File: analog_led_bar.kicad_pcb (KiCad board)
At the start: 2 copper layers, 71.4 x 22 mm, 13 parts, among them P1 SIG, U1 OPAMP_DR, U2 LM3914, U3 LM3914

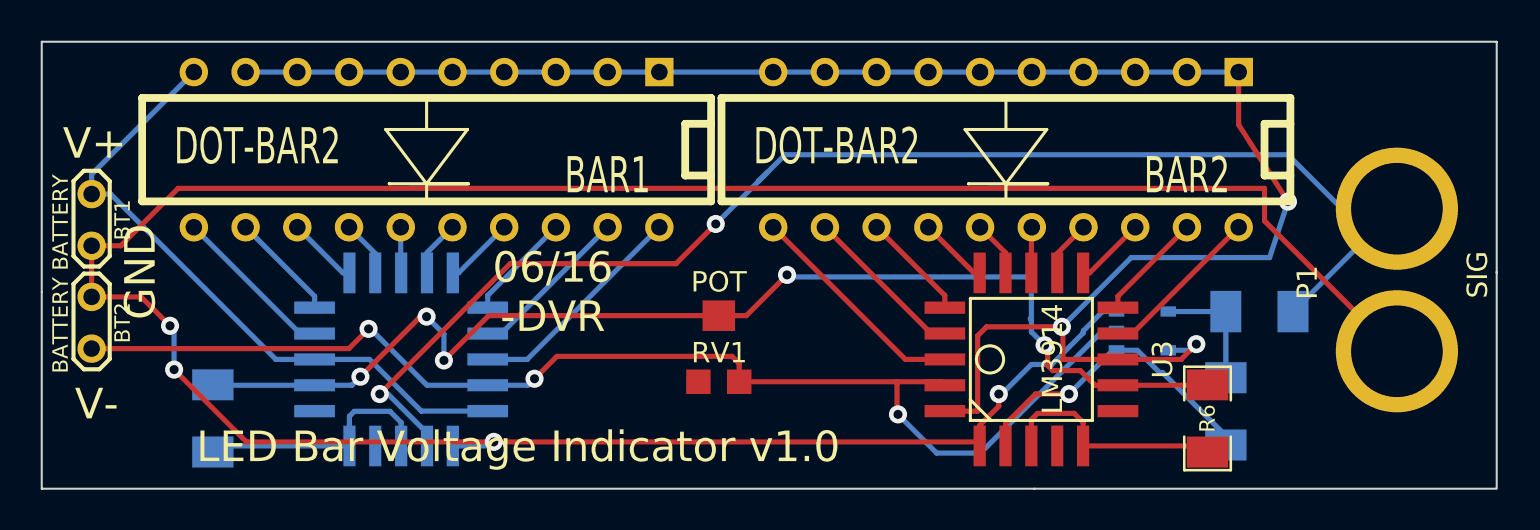
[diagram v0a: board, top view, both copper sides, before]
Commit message: Fixed unconnected nodes. Now v1.1. Confirmed works if variable resistor is set properly.
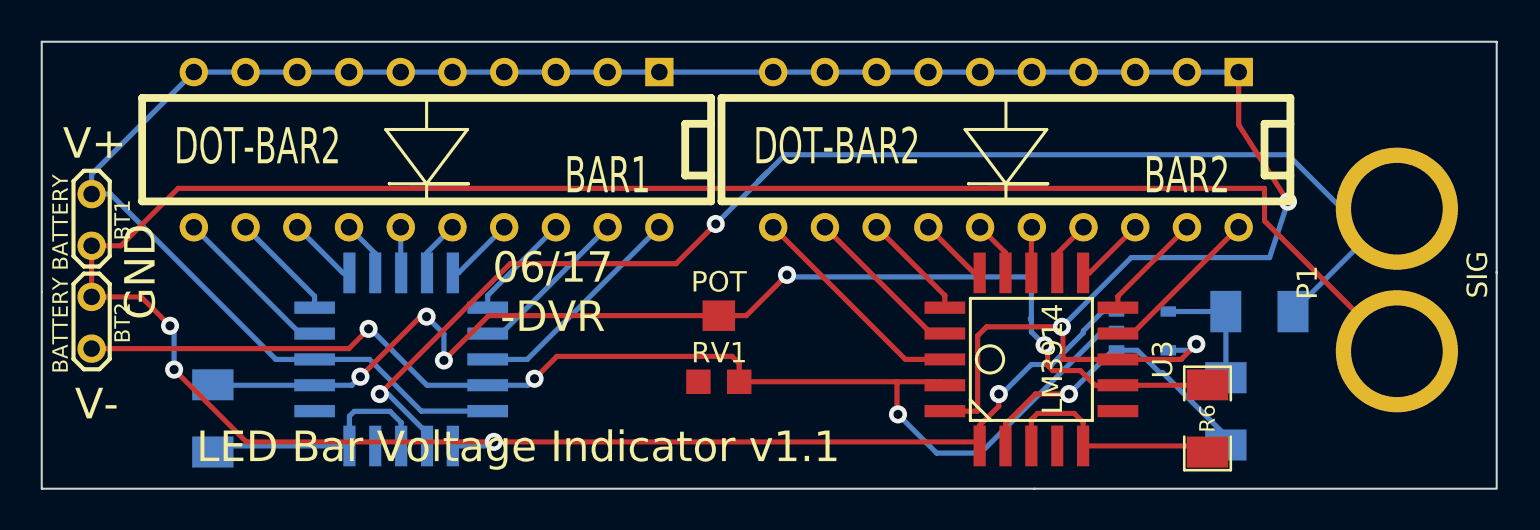
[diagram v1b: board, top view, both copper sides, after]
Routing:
- net /Vcc: track 121.9 -> 124.4 mm
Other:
- board text added: "06/17 -DVR"
- board text added: "LED Bar Voltage Indicator v1.1"
- board text removed: "06/16 -DVR"
- board text removed: "LED Bar Voltage Indicator v1.0"
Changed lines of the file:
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@@
   (general
     (links 68)
-    (no_connects 1)
+    (no_connects 0)
     (area 22.299999 12.699999 93.850001 34.750001)
     (thickness 1.6)
     (drawings 13)
-    (tracks 221)
+    (tracks 222)
     (zones 0)
     (modules 13)
@@
     (pad_to_mask_clearance 0)
     (aux_axis_origin 0 0)
-    (visible_elements FFFFFFBF)
+    (visible_elements 7FFFFFFF)
     (pcbplotparams
       (layerselection 285179905)
@@
     )
   )
-  (gr_text "06/16\n-DVR" (at 47.45 25.05) (layer F.SilkS)
+  (gr_text "06/17\n-DVR" (at 47.45 25.05) (layer F.SilkS)
     (effects (font (size 1.5 1.5) (thickness 0.3)))
   )
-  (gr_text "LED Bar Voltage Indicator v1.0" (at 45.75 32.65) (layer F.SilkS)
+  (gr_text "LED Bar Voltage Indicator v1.1" (at 45.75 32.65) (layer F.SilkS)
     (effects (font (size 1.5 1.5) (thickness 0.3)))
   )
@@
   (segment (start 41.27 31.97) (end 39.35 30.05) (width 0.254) (layer B.Cu) (net 23))
   (segment (start 88.6 19.15) (end 90.45 21) (width 0.254) (layer B.Cu) (net 23))
-  (segment (start 57.55 19.6) (end 58 19.15) (width 0.254) (layer B.Cu) (net 23) (status 2))
+  (segment (start 57.55 19.6) (end 58 19.15) (width 0.254) (layer B.Cu) (net 23))
   (segment (start 69.68 32.6) (end 69.68 31.52) (width 0.254) (layer F.Cu) (net 24))
   (segment (start 74.9475 27.9025) (end 75.13 27.9025) (width 0.254) (layer B.Cu) (net 24))
@@
   (segment (start 77.25 29) (end 77.4 29) (width 0.254) (layer B.Cu) (net 24))
   (segment (start 76.1525 27.9025) (end 77.25 29) (width 0.254) (layer B.Cu) (net 24))
+  (segment (start 29.82 14.24) (end 32.36 14.24) (width 0.254) (layer B.Cu) (net 25) (status C00000))
   (segment (start 24.8 20.23) (end 24.8 19.26) (width 0.254) (layer B.Cu) (net 25))
   (segment (start 24.8 19.26) (end 29.82 14.24) (width 0.254) (layer B.Cu) (net 25))
